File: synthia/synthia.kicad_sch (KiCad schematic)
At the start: 119 parts, among them J1 MJ-63022B, J2 SJ3-35083C-TR, J3 PJ-007, J4 SDS-50J, Q1 IRF9540N, U1 TLV272IP, U2 STM32H750ZBT6, U3 LD1117V33, U4 PVA1EEH31.2NV2, U5 PVA1EEH31.2NV2, U6 ATS08A-E

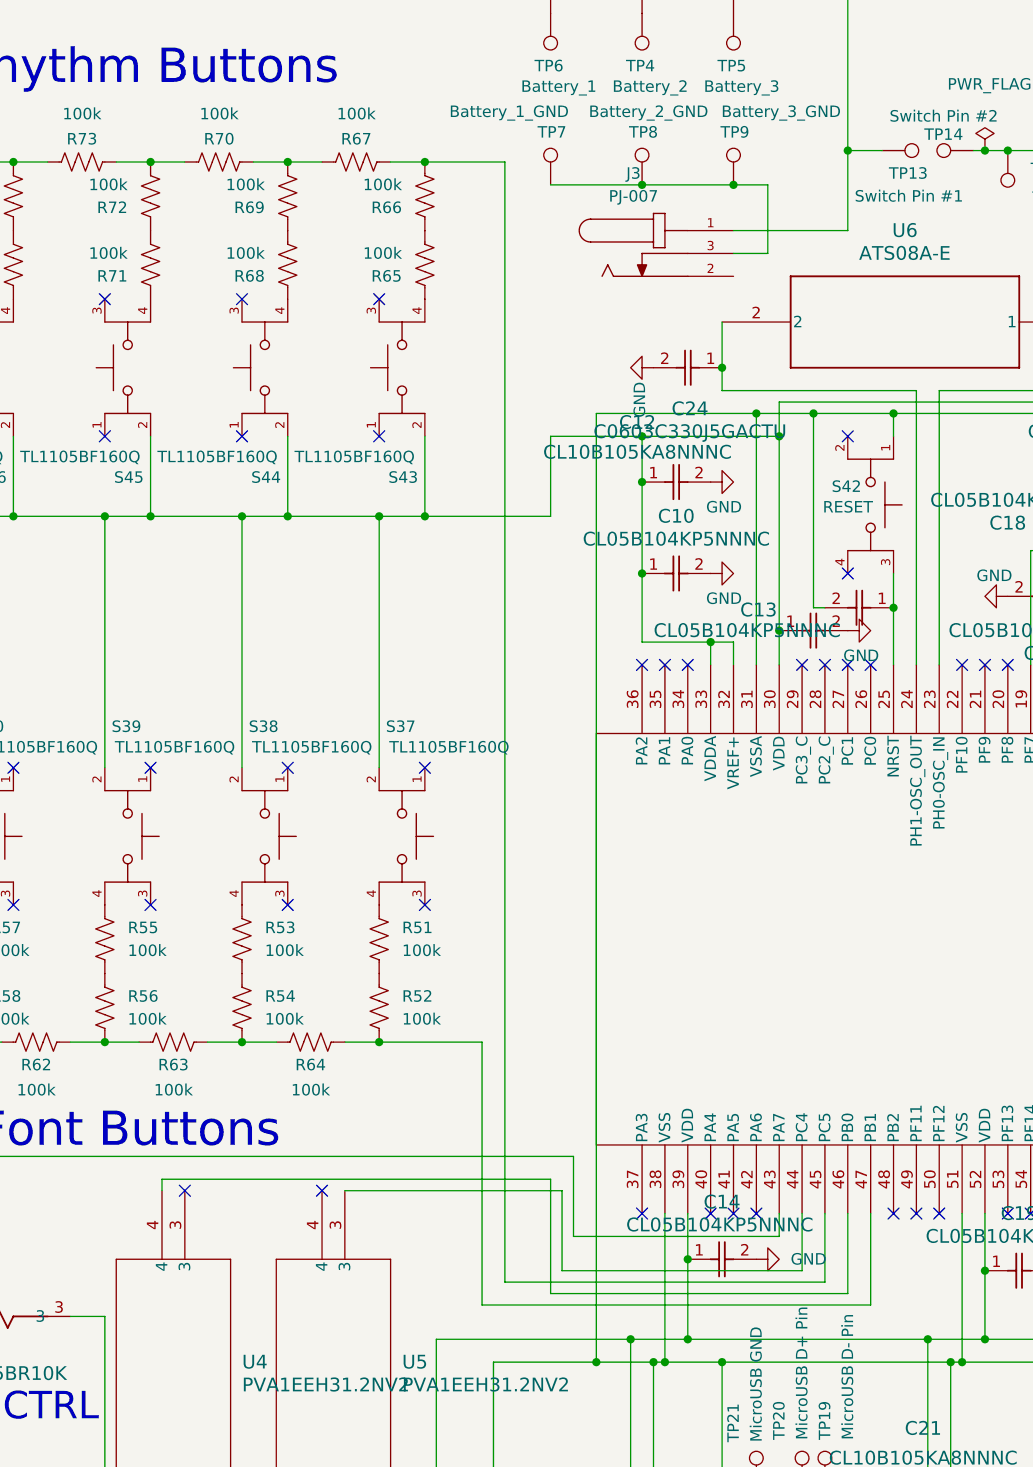
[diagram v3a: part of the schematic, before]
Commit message: PCB Revision 1.0 complete, Ground zones are filled, all components are wired, and holes are made for standoffs for case installment. Final changes to the onshape will need to be made to accomodate the pcb design
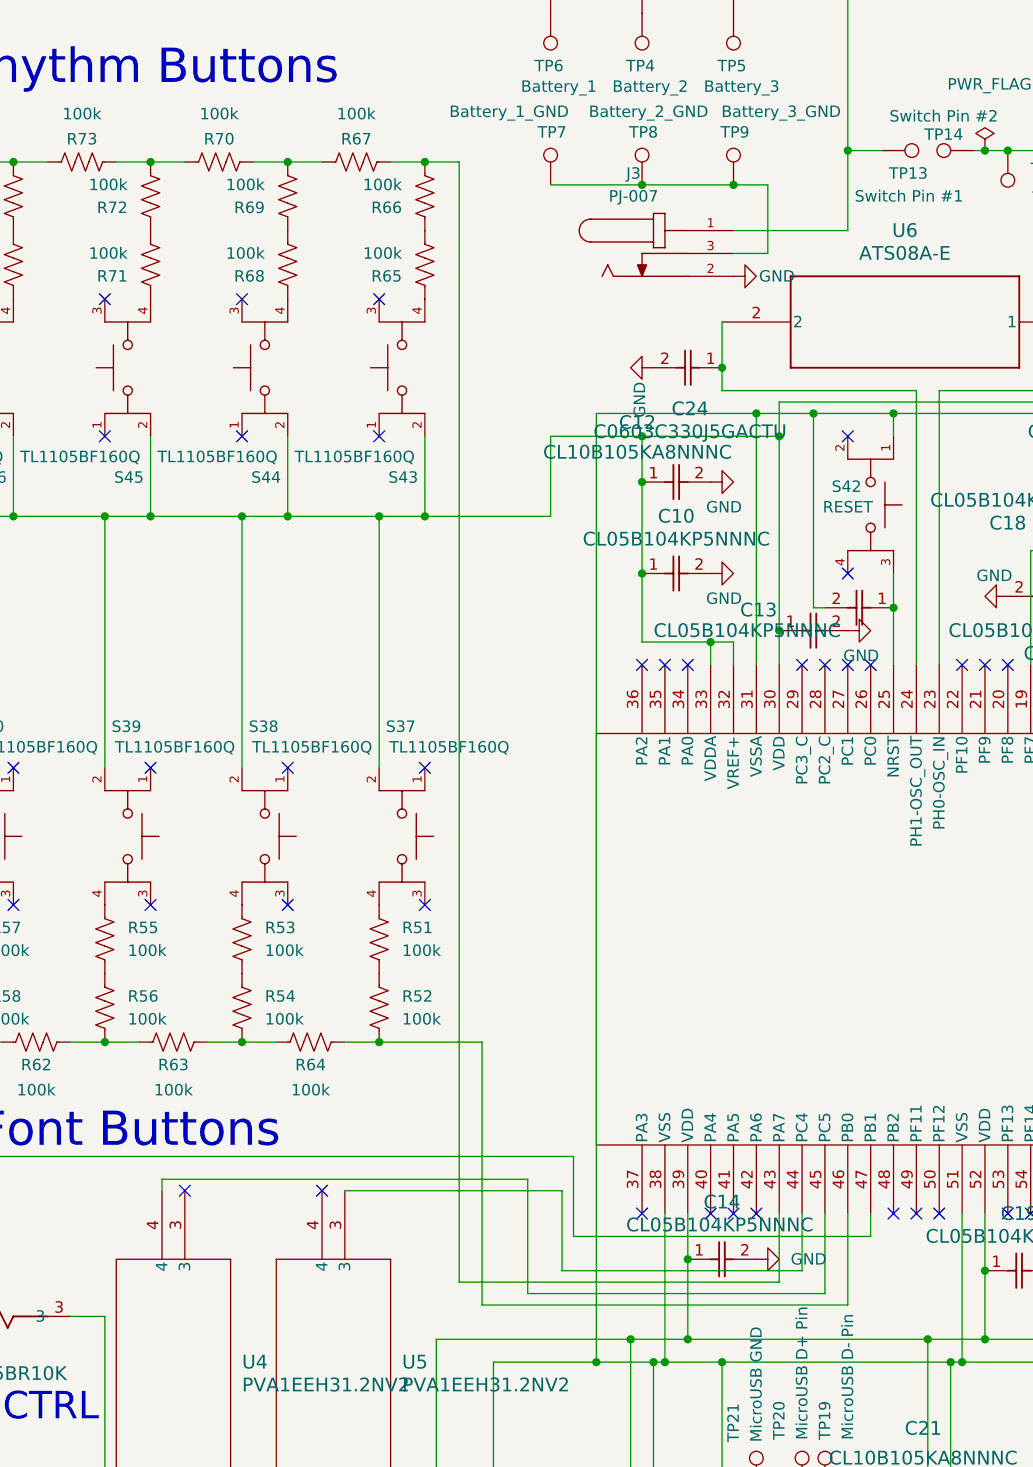
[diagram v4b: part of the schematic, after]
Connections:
- net GND: now also J3.2
- net at R66.2, R67.1: now also U2.43 (PA7); no longer U2.45 (PC5)
- net at R52.2, R64.2: now also U2.46 (PB0); no longer U2.47 (PB1)
- net at U4.4: now also U2.45 (PC5); no longer U2.46 (PB0)
- net at R79.2: now also U2.47 (PB1); no longer U2.43 (PA7)
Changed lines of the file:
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@@
 	(wire
 		(pts
-			(xy 82.55 44.45) (xy 91.44 44.45)
+			(xy 82.55 44.45) (xy 86.36 44.45)
 		)
 		(stroke
@@
 	(wire
 		(pts
+			(xy 129.54 161.29) (xy 129.54 171.45)
+		)
+		(stroke
+			(width 0)
+			(type default)
+		)
+	)
+	(wire
+		(pts
 			(xy 162.56 91.44) (xy 240.03 91.44)
 		)
@@
 	(wire
 		(pts
-			(xy 127 168.91) (xy 127 161.29)
-		)
-		(stroke
-			(width 0)
-			(type default)
-		)
-	)
-	(wire
-		(pts
 			(xy 129.54 43.18) (xy 129.54 52.07)
 		)
@@
 	(wire
 		(pts
-			(xy 129.54 20.32) (xy 129.54 43.18)
+			(xy 121.92 161.29) (xy 121.92 168.91)
 		)
 		(stroke
@@
 	(wire
 		(pts
-			(xy 236.22 125.73) (xy 246.38 125.73)
+			(xy 129.54 20.32) (xy 129.54 43.18)
 		)
 		(stroke
@@
 	(wire
 		(pts
-			(xy 73.66 199.39) (xy 73.66 200.66)
+			(xy 236.22 125.73) (xy 246.38 125.73)
 		)
 		(stroke
@@
 	(wire
 		(pts
-			(xy 121.92 71.12) (xy 121.92 74.93)
+			(xy 73.66 199.39) (xy 73.66 200.66)
 		)
 		(stroke
@@
 	(wire
 		(pts
-			(xy 31.75 83.82) (xy 31.75 111.76)
+			(xy 121.92 71.12) (xy 121.92 74.93)
 		)
 		(stroke
@@
 	(wire
 		(pts
-			(xy 132.08 171.45) (xy 132.08 161.29)
+			(xy 31.75 83.82) (xy 31.75 111.76)
 		)
 		(stroke
@@
 	(wire
 		(pts
-			(xy 91.44 168.91) (xy 127 168.91)
+			(xy 86.36 168.91) (xy 121.92 168.91)
 		)
 		(stroke
@@
 	(wire
 		(pts
+			(xy 132.08 163.83) (xy 132.08 161.29)
+		)
+		(stroke
+			(width 0)
+			(type default)
+		)
+	)
+	(wire
+		(pts
 			(xy 157.48 303.53) (xy 247.65 303.53)
 		)
@@
 	(wire
 		(pts
-			(xy 96.52 157.48) (xy 96.52 170.18)
+			(xy 93.98 157.48) (xy 93.98 170.18)
 		)
 		(stroke
@@
 	(wire
 		(pts
-			(xy 88.9 171.45) (xy 132.08 171.45)
+			(xy 88.9 171.45) (xy 129.54 171.45)
 		)
 		(stroke
@@
 	(wire
 		(pts
-			(xy 53.34 157.48) (xy 96.52 157.48)
+			(xy 53.34 157.48) (xy 93.98 157.48)
 		)
 		(stroke
@@
 	(wire
 		(pts
-			(xy 129.54 170.18) (xy 129.54 161.29)
-		)
-		(stroke
-			(width 0)
-			(type default)
-		)
-	)
-	(wire
-		(pts
 			(xy 167.64 177.8) (xy 168.91 177.8)
 		)
@@
 	(wire
 		(pts
-			(xy 96.52 170.18) (xy 129.54 170.18)
+			(xy 93.98 170.18) (xy 127 170.18)
 		)
 		(stroke
@@
 	(wire
 		(pts
-			(xy 99.06 163.83) (xy 121.92 163.83)
+			(xy 99.06 163.83) (xy 132.08 163.83)
 		)
 		(stroke
@@
 	(wire
 		(pts
-			(xy 91.44 44.45) (xy 91.44 168.91)
+			(xy 86.36 44.45) (xy 86.36 168.91)
 		)
 		(stroke
@@
 	(wire
 		(pts
-			(xy 115.57 67.31) (xy 115.57 69.85)
+			(xy 127 161.29) (xy 127 170.18)
 		)
 		(stroke
@@
 	(wire
 		(pts
-			(xy 62.23 142.24) (xy 66.04 142.24)
+			(xy 115.57 67.31) (xy 115.57 69.85)
 		)
 		(stroke
@@
 	(wire
 		(pts
-			(xy 101.6 177.8) (xy 107.95 177.8)
+			(xy 62.23 142.24) (xy 66.04 142.24)
 		)
 		(stroke
@@
 	(wire
 		(pts
-			(xy 107.95 177.8) (xy 109.22 177.8)
+			(xy 101.6 177.8) (xy 107.95 177.8)
 		)
 		(stroke
@@
 	(wire
 		(pts
-			(xy 238.76 66.04) (xy 222.25 66.04)
+			(xy 107.95 177.8) (xy 109.22 177.8)
 		)
 		(stroke
@@
 	(wire
 		(pts
-			(xy 120.65 54.61) (xy 120.65 46.99)
+			(xy 238.76 66.04) (xy 222.25 66.04)
 		)
 		(stroke
@@
 	(wire
 		(pts
-			(xy 170.18 95.25) (xy 236.22 95.25)
+			(xy 120.65 54.61) (xy 120.65 46.99)
 		)
 		(stroke
@@
 	(wire
 		(pts
-			(xy 171.45 43.18) (xy 184.15 43.18)
+			(xy 170.18 95.25) (xy 236.22 95.25)
 		)
 		(stroke
@@
 	(wire
 		(pts
-			(xy 121.92 163.83) (xy 121.92 161.29)
+			(xy 171.45 43.18) (xy 184.15 43.18)
 		)
 		(stroke
@@
 					(unit 1)
 				)
+			)
+		)
+	)
+	(symbol
+		(lib_id "power:GND")
+		(at 116.84 57.15 90)
+		(unit 1)
+		(body_style 1)
+		(exclude_from_sim no)
+		(in_bom yes)
+		(on_board yes)
+		(in_pos_files yes)
+		(dnp no)
+		(property "Reference" "#PWR046"
+			(at 123.19 57.15 0)
+			(hide yes)
+			(show_name no)
+			(do_not_autoplace no)
+			(effects
+				(font
+					(size 1.27 1.27)
+				)
+			)
+		)
+		(property "Value" "GND"
+			(at 121.666 57.15 90)
+			(show_name no)
+			(do_not_autoplace no)
+			(effects
+				(font
+					(size 1.27 1.27)
+				)
+			)
+		)
+		(property "Footprint" ""
+			(at 116.84 57.15 0)
+			(hide yes)
+			(show_name no)
+			(do_not_autoplace no)
+			(effects
+				(font
+					(size 1.27 1.27)
+				)
+			)
+		)
+		(property "Datasheet" ""
+			(at 116.84 57.15 0)
+			(hide yes)
+			(show_name no)
+			(do_not_autoplace no)
+			(effects
+				(font
+					(size 1.27 1.27)
+				)
+			)
+		)
+		(property "Description" "Power symbol creates a global label with name \"GND\" , ground"
+			(at 116.84 57.15 0)
+			(hide yes)
+			(show_name no)
+			(do_not_autoplace no)
+			(effects
+				(font
+					(size 1.27 1.27)
+				)
+			)
+		)
+		(pin "1"
+		)
+		(instances
+			(project "synthia"
+				(path "/b7ca07b0-c23c-4333-a610-582d2798793b"
+					(reference "#PWR046")
+					(unit 1)
+				)
